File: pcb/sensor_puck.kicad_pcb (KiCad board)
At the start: 2 copper layers, 41.6 x 41.9 mm, 35 parts, among them J1 Conn_01x07_Socket, J2 Conn_01x07_Socket, J3 USB_C_Receptacle_USB2.0_16P, SW1 RST, SW2 BOOT, U1 ESP32-S3-MINI-1U, U2 LIS3MDL, U3 LSM6DSOXTR, U4 STC31-C-R3

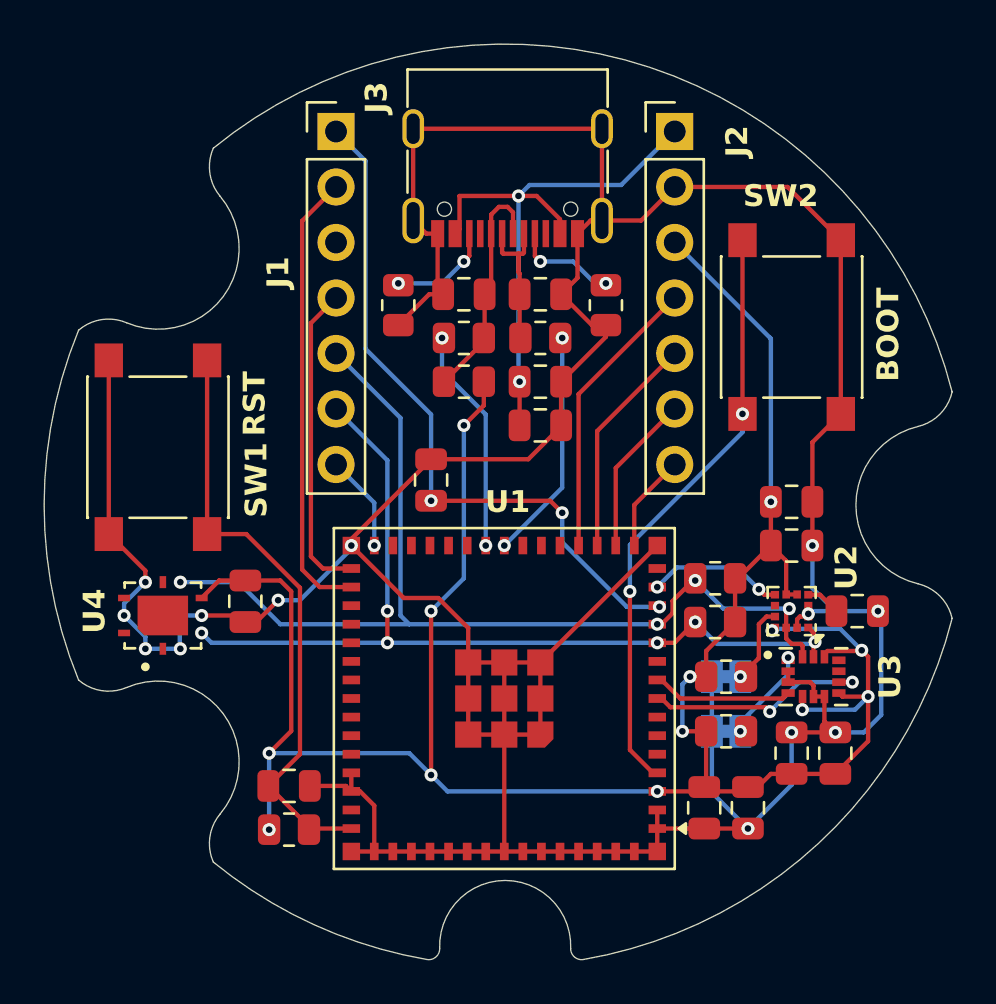
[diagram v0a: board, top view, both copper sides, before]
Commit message: fix(pcb): improve USB-C wiring and routing
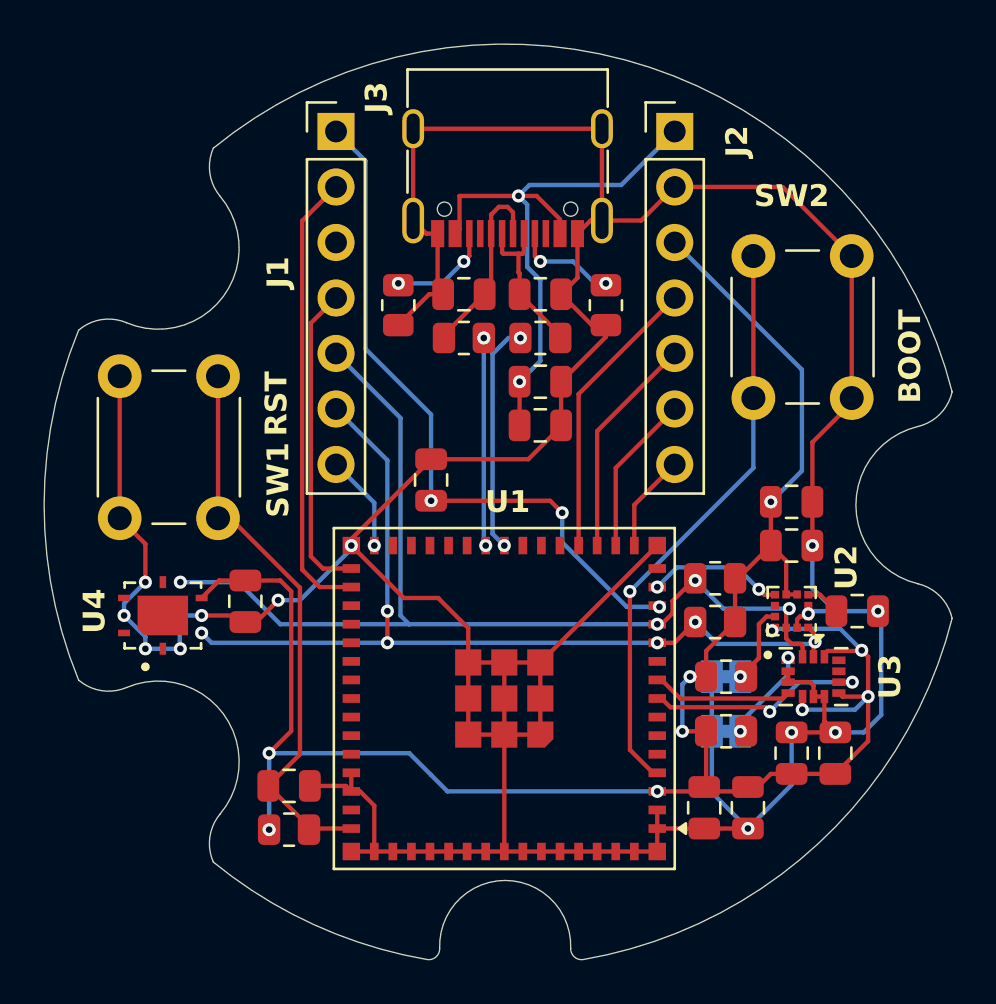
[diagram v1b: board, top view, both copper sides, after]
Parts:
- removed R7: 10k, Resistor_SMD:R_0805_2012Metric
- C4, C5: value C -> DNP
- R8, R9: value 0 -> 22R
- SW1, SW2: footprint Button_Switch_SMD:SW_Push_1P1T_NO_6x6mm_H9.5mm -> Button_Switch_THT:SW_PUSH_6mm
- moved SW2 4.26 mm to (115.8, 88.8)
- moved SW1 3.69 mm to (82.2, 100.8)
- turned R8 to 180 degrees
- turned R9 to 180 degrees
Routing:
- net +3V3: track 113.4 -> 95.6 mm, vias 13 -> 10
- net Net-(C4-Pad1): track 10.8 -> 8.85 mm
- net Net-(U1-EN): track 27.7 -> 26.0 mm
- net GND: track 201.9 -> 200.3 mm
- net Net-(C5-Pad1): track 6.67 -> 7.52 mm
- net +5V: track 26.4 -> 27.2 mm
- net USB_D+: track 10.4 -> 9.76 mm
- net Net-(U1-IO0): track 27.1 -> 26.6 mm, vias 2 -> 1
